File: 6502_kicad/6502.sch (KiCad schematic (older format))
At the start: 19 parts, among them J1 Conn_01x02, J2 Conn_02x10_Odd_Even, J3 Conn_02x10_Odd_Even, J4 Conn_01x08, U1 24LC256, U10 74HC04, U11 W65C51N, U12 WD65C22, U13 WD65C22, U14 74LS138, U2 74HC595, U3 WD65C02, U4 628128, U5 74HC595, U6 ATmega328P-PU, U7 74LS30, U8 74HC595, U9 74LS08

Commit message: Working on kicad.
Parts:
- removed J1: Conn_01x02, Connector_PinHeader_1.00mm:PinHeader_1x02_P1.00mm_Vertical, symbol Connector_Generic:Conn_01x02
- removed J2, J3: Conn_02x10_Odd_Even, Connector_PinHeader_1.00mm:PinHeader_2x10_P1.00mm_Vertical, symbol Connector_Generic:Conn_02x10_Odd_Even
- removed J4: Conn_01x08, Connector_PinHeader_1.27mm:PinHeader_1x08_P1.27mm_Vertical, symbol Connector_Generic:Conn_01x08
- removed U1: 24LC256, Package_DIP:DIP-8_W7.62mm, symbol Memory_EEPROM:24LC256
- removed U10: 74HC04, Package_DIP:DIP-14_W7.62mm, symbol 74xx:74HC04
- removed U11: W65C51N, Package_DIP:DIP-28_W15.24mm, symbol 65xx:W65C51N
- removed U12, U13: WD65C22, Package_DIP:DIP-40_W15.24mm, symbol 65xx:WD65C22
- removed U14: 74LS138, Package_DIP:DIP-16_W7.62mm, symbol 74xx:74LS138
- removed U2, U5, U8: 74HC595, Package_DIP:DIP-16_W7.62mm, symbol 74xx:74HC595
- removed U3: WD65C02, Package_DIP:DIP-40_W15.24mm, symbol 65xx:WD65C02
- removed U4: 628128, Package_DIP:DIP-32_W15.24mm, symbol Memory_RAM:628128
- removed U6: ATmega328P-PU, Package_DIP:DIP-28_W7.62mm, symbol MCU_Microchip_ATmega:ATmega328P-PU
- removed U7: 74LS30, Package_DIP:DIP-14_W7.62mm, symbol 74xx:74LS30
- removed unit 2 of U9
- added A1: Arduino_Nano_v2.x, Module:Arduino_Nano, symbol MCU_Module:Arduino_Nano_v2.x
- added R2, R3, R4, R5: 3.3K, Resistor_THT:R_Axial_DIN0204_L3.6mm_D1.6mm_P5.08mm_Horizontal, symbol Device:R
- added U1: WD65C02, Package_DIP:DIP-40_W15.24mm, symbol 65xx:WD65C02
- added U10: 74LS04, Package_DIP:DIP-14_W7.62mm, symbol 74xx:74LS04
- added U11: 74LS138, Package_DIP:DIP-16_W7.62mm, symbol 74xx:74LS138
- added U2: 628128, Package_DIP:DIP-32_W15.24mm, symbol Memory_RAM:628128
- added U3: 24C256, Package_DIP:DIP-8_W7.62mm, symbol Memory_EEPROM:CAT24C256
- added U5, U6, U7: 74HCT595, Package_DIP:DIP-16_W7.62mm, symbol 74xx:74HCT595
- added U8: 74LS30, Package_DIP:DIP-14_W7.62mm, symbol 74xx:74LS30
- added unit 3 of U9
- added unit 4 of U9
- added X1: CXO_DIP14, Oscillator:Oscillator_DIP-14, symbol Oscillator:CXO_DIP14
- R1: value 1K -> 3.3K; footprint Resistor_THT:R_Axial_DIN0207_L6.3mm_D2.5mm_P7.62mm_Horizontal -> Resistor_THT:R_Axial_DIN0204_L3.6mm_D1.6mm_P5.08mm_Horizontal
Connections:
- net +5V: now also A1.30 (VIN), R2.2, R3.2, R4.2, R5.2, U1.38 (~SO), U1.8 (VCC), U11.16 (VCC), U2.32 (VCC), U3.7 (WP), U3.8 (VCC), U5.16 (VCC), U6.16 (VCC), U7.16 (VCC), X1.14 (Vcc)
- net GND: now also A1.29 (GND), A1.4 (GND), U1.21 (GND), U11.4 (E1), U11.5 (E2), U11.8 (GND), U2.16 (GND), U2.2 (A16), U3.1 (A0), U3.2 (A1), U3.3 (A2), U3.4 (GND), U5.8 (GND), U6.8 (GND), U7.8 (GND), X1.7 (GND)
- net a0: now also U1.9 (A0), U2.12 (A0), U6.7 (QH)
- net a1: now also U1.10 (A1), U2.11 (A1), U6.6 (QG)
- net a10: now also U1.19 (A10), U2.23 (A10), U7.5 (QF), U8.6
- net a11: now also U1.20 (A11), U2.25 (A11), U7.4 (QE), U8.5
- net a12: now also U1.22 (A12), U2.4 (A12), U7.3 (QD), U8.4
- net a13: now also U1.23 (A13), U2.28 (A13), U7.2 (QC), U8.3
- net a14: now also U1.24 (A14), U2.3 (A14), U7.1 (QB), U8.2
- net a15: now also U1.25 (A15), U2.31 (A15), U7.15 (QA), U8.1
- net a2: now also U1.11 (A2), U2.10 (A2), U6.5 (QF)
- net a3: now also U1.12 (A3), U2.9 (A3), U6.4 (QE)
- net a4: now also U1.13 (A4), U11.1 (A0), U2.8 (A4), U6.3 (QD)
- net a5: now also U1.14 (A5), U11.2 (A1), U2.7 (A5), U6.2 (QC)
- net a6: now also U1.15 (A6), U11.3 (A2), U2.6 (A6), U6.1 (QB)
- net a7: now also U1.16 (A7), U10.1, U2.5 (A7), U6.15 (QA)
- net a8: now also U1.17 (A8), U2.27 (A8), U7.7 (QH), U8.12
- net a9: now also U1.18 (A9), U2.26 (A9), U7.6 (QG), U8.11
- net d0: now also U1.33 (D0), U2.13 (Q0), U5.15 (QA)
- net d1: now also U1.32 (D1), U2.14 (Q1), U5.1 (QB)
- net d2: now also U1.31 (D2), U2.15 (Q2), U5.2 (QC)
- net d3: now also U1.30 (D3), U2.17 (Q3), U5.3 (QD)
- net d4: now also U1.29 (D4), U2.18 (Q4), U5.4 (QE)
- net d5: now also U1.28 (D5), U2.19 (Q5), U5.5 (QF)
- net d6: now also U1.27 (D6), U2.20 (Q6), U5.6 (QG)
- net d7: now also U1.26 (D7), U2.21 (Q7), U5.7 (QH)
- net ~CS_RAM: now reaches U9.3
- net ~CS_RAM: now also U10.5, U2.22 (CS1), U2.24 (OE)
- net at R1.1: now also U1.40 (~RESET)
- net at U9.2: now also U10.2
- net at U9.1: now also U10.4
- new net: R2.1, U1.2 (RDY)
- new net: R3.1, U1.4 (~IRQ)
- new net: R4.1, U1.6 (~NMI)
- new net: U1.37 (PHI2), X1.8 (OUT)
- new net: A1.8 (D5), U1.34 (R/~W), U2.29 (WR)
- new net: A1.23 (A4), U3.5 (SDA)
- new net: A1.24 (A5), U3.6 (SCL)
- new net: A1.6 (D3), U5.11 (SRCLK), U6.11 (SRCLK), U7.11 (SRCLK)
- new net: A1.7 (D4), U5.12 (RCLK), U6.12 (RCLK), U7.12 (RCLK)
- new net: U5.14 (SER), U6.9 (QH')
- new net: U6.14 (SER), U7.9 (QH')
- new net: A1.5 (D2), U7.14 (SER)
- new net: U10.3, U8.8
- new net Bus_Enable: A1.9 (D6), R5.1, U1.36 (BE), U5.13 (~OE), U6.13 (~OE), U7.13 (~OE)
- new net CS_IO: U10.6, U11.6 (E3)
- new net phi2out: U1.39 (PHI2out), U2.30 (CS2)
- no-connect marks 7 -> 5

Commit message: Last commit before changing to ROM/RAM configuration.
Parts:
- A1: symbol MCU_Module:Arduino_Nano_v2.x -> 6502-rescue:Arduino_Nano_v2.x-MCU_Module
- U2: symbol Memory_RAM:628128 -> 6502-rescue:628128-Memory_RAM
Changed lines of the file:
@@
 EESchema Schematic File Version 4
-LIBS:6502-cache
-EELAYER 26 0
+EELAYER 30 0
 EELAYER END
 $Descr USLedger 17000 11000
@@
 $EndComp
 $Comp
-L Memory_RAM:628128 U2
+L 6502-rescue:628128-Memory_RAM U2
 U 1 1 5F31F682
 P 5400 2400
@@
 	12350 1050 12350 850
 $Comp
-L MCU_Module:Arduino_Nano_v2.x A1
+L 6502-rescue:Arduino_Nano_v2.x-MCU_Module A1
 U 1 1 5F3207EB
 P 10300 2350

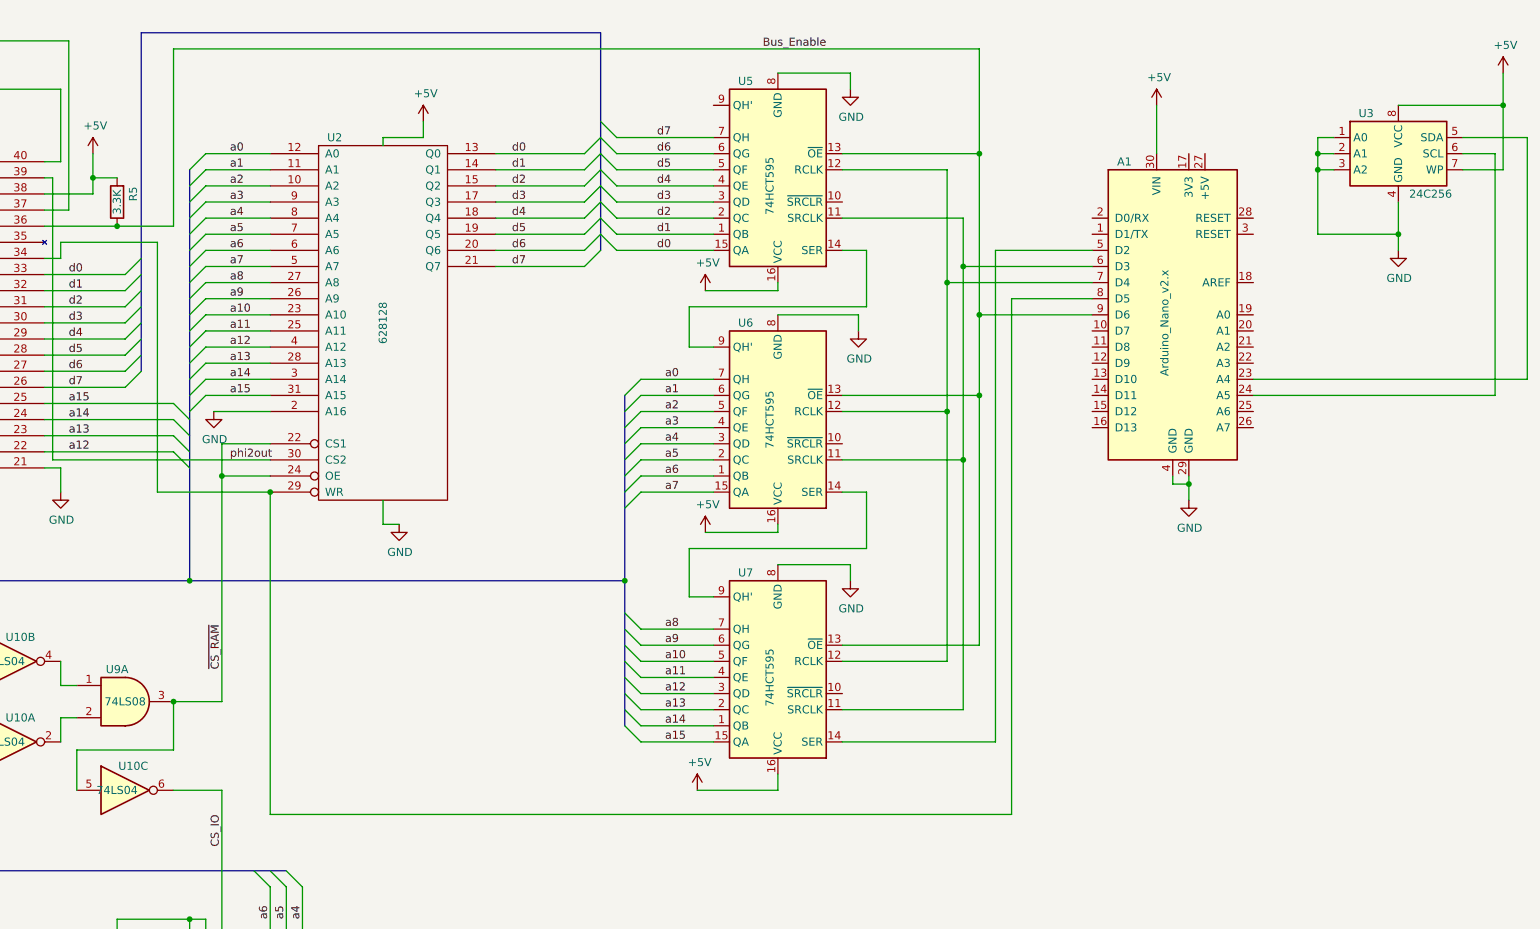
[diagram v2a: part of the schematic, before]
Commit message: Start working on interrupt section of Ben's videos.
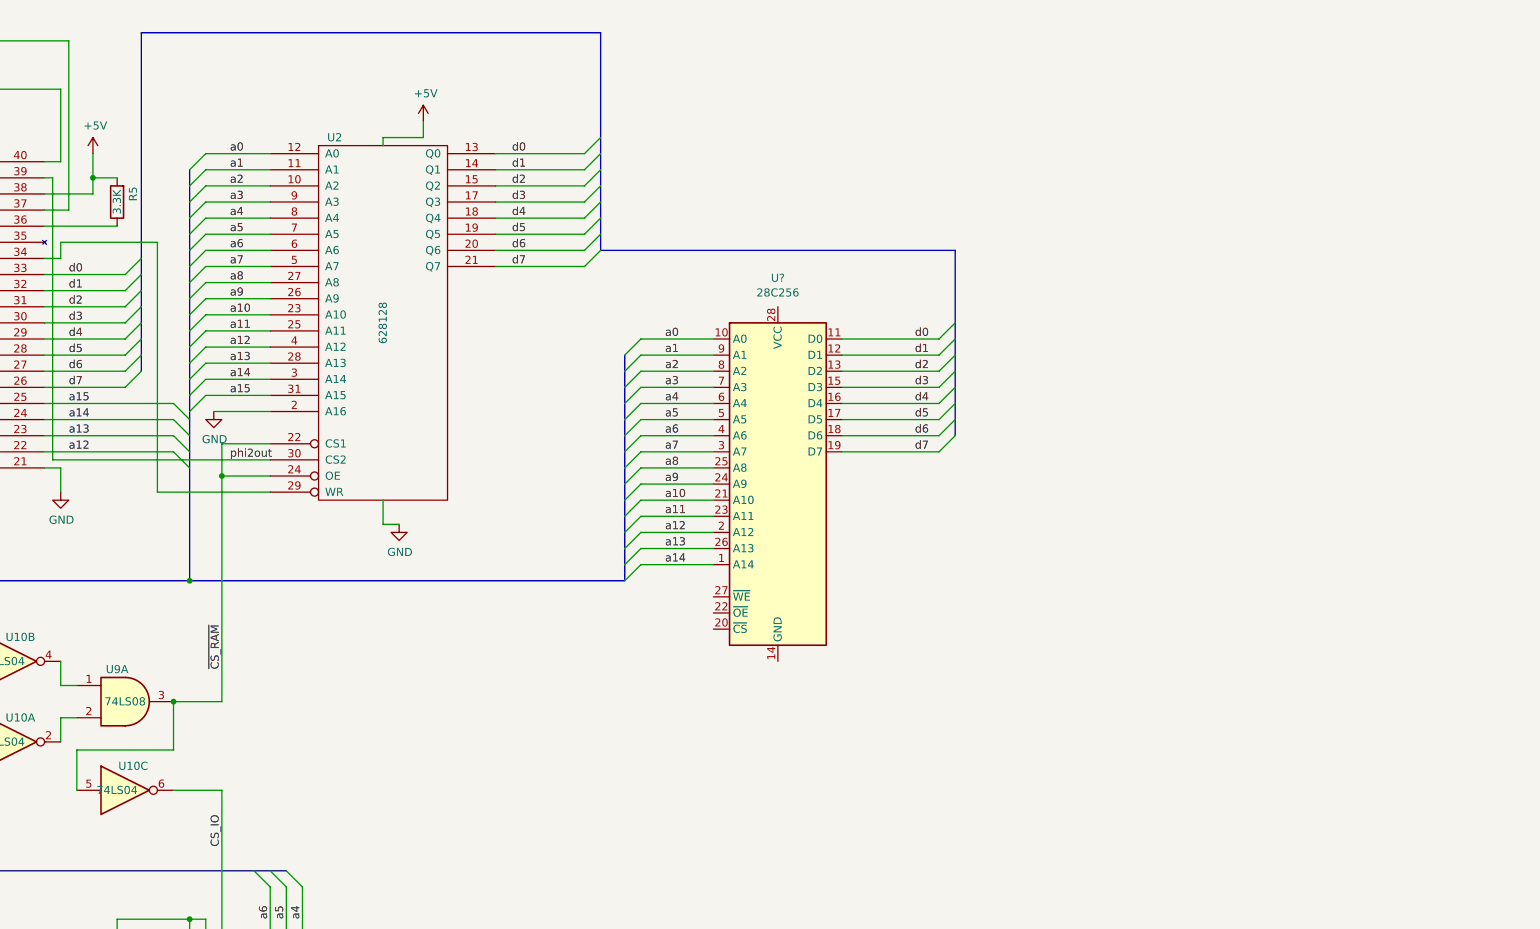
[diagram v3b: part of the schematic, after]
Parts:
- removed A1: Arduino_Nano_v2.x, Module:Arduino_Nano, symbol 6502-rescue:Arduino_Nano_v2.x-MCU_Module
- removed U3: 24C256, Package_DIP:DIP-8_W7.62mm, symbol Memory_EEPROM:CAT24C256
- removed U5, U6, U7: 74HCT595, Package_DIP:DIP-16_W7.62mm, symbol 74xx:74HCT595
- added U?: 28C256, symbol Memory_EEPROM:28C256
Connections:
- net a0: now also U?.10 (A0)
- net a1: now also U?.9 (A1)
- net a10: now also U?.21 (A10)
- net a11: now also U?.23 (A11)
- net a12: now also U?.2 (A12)
- net a13: now also U?.26 (A13)
- net a14: now also U?.1 (A14)
- net a2: now also U?.8 (A2)
- net a3: now also U?.7 (A3)
- net a4: now also U?.6 (A4)
- net a5: now also U?.5 (A5)
- net a6: now also U?.4 (A6)
- net a7: now also U?.3 (A7)
- net a8: now also U?.25 (A8)
- net a9: now also U?.24 (A9)
- net d0: now also U?.11 (D0)
- net d1: now also U?.12 (D1)
- net d2: now also U?.13 (D2)
- net d3: now also U?.15 (D3)
- net d4: now also U?.16 (D4)
- net d5: now also U?.17 (D5)
- net d6: now also U?.18 (D6)
- net d7: now also U?.19 (D7)
- net Bus_Enable: no longer names the net of R5.1, U1.36 (BE)
